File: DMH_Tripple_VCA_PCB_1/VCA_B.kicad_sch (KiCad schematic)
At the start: 19 parts, among them Q3 BC548, Q4 BC548, U1 TL074

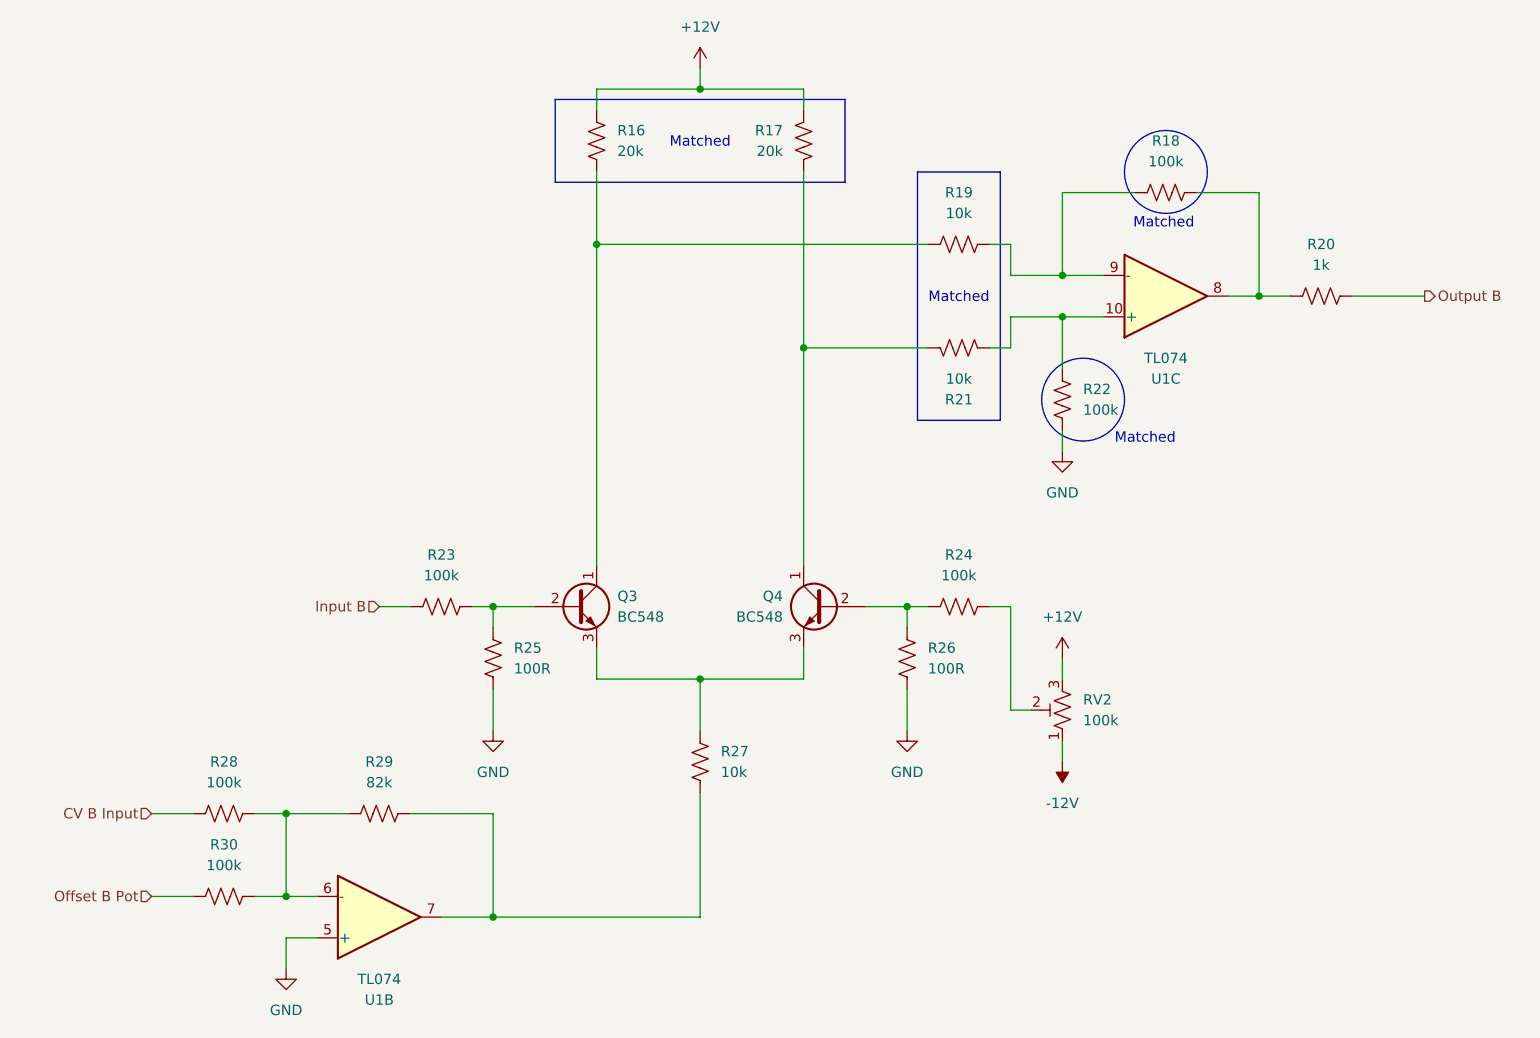
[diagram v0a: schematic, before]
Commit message: PCB 1 component positioning in progress
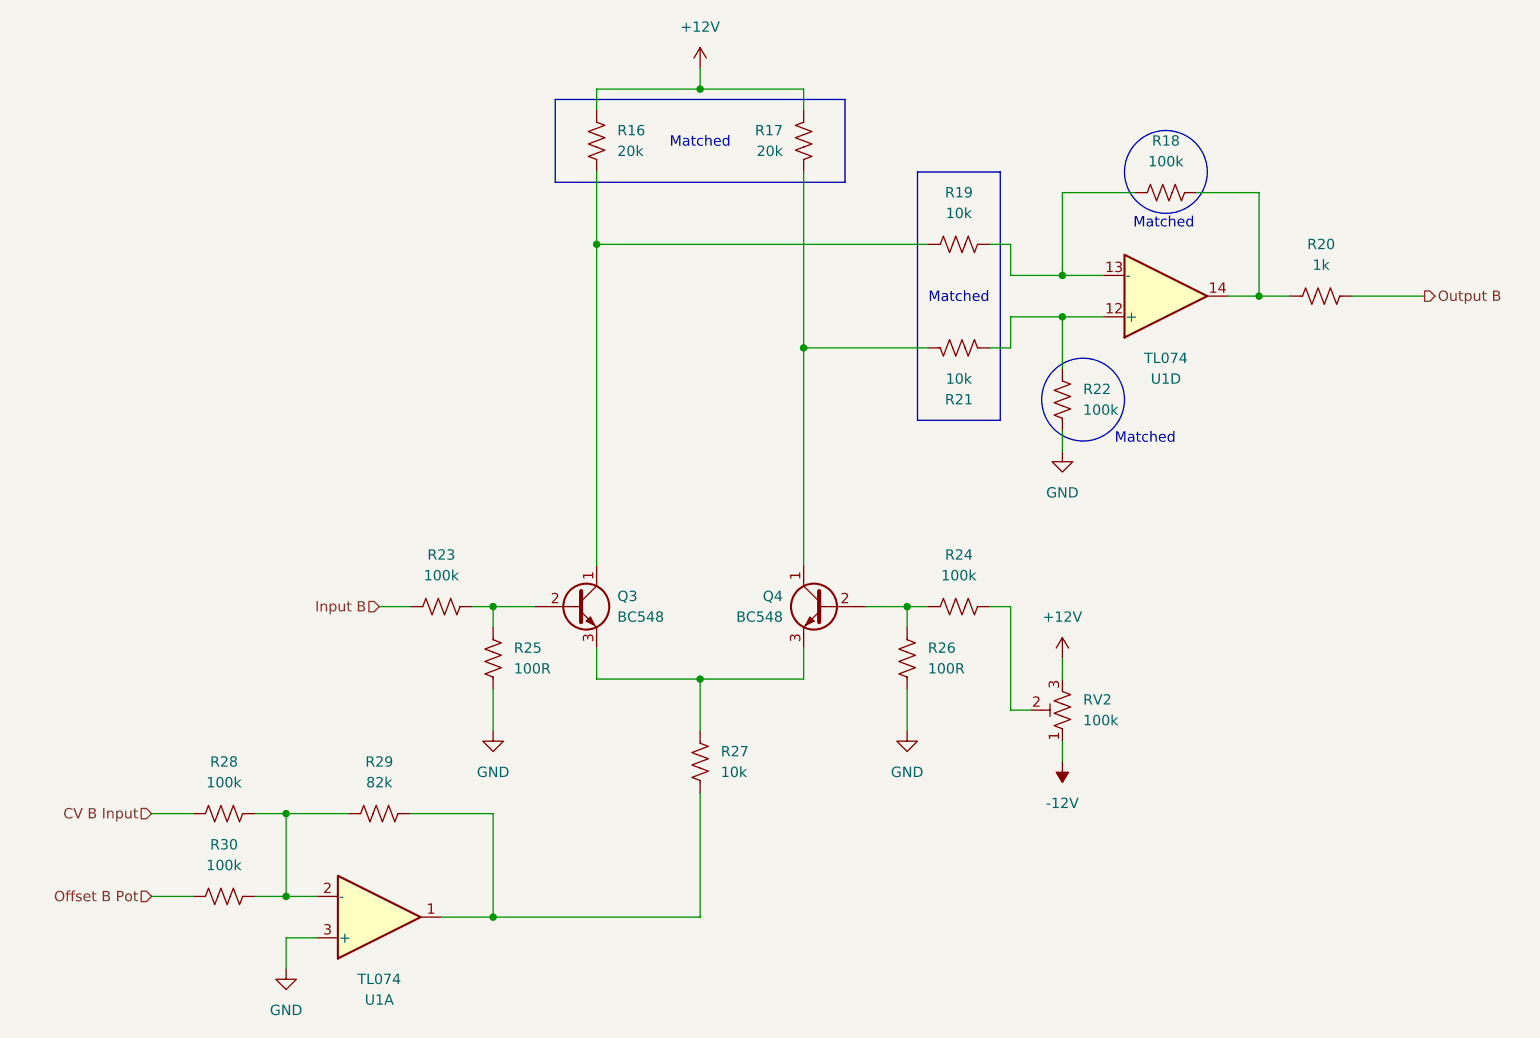
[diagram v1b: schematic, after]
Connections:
- net GND: now also U1.3 (+); no longer U1.5 (+)
- net at R18.1, R20.2: now also U1.14; no longer U1.8
- net at R18.2, R19.1: now also U1.13 (-); no longer U1.9 (-)
- net at R21.1, R22.1: now also U1.12 (+); no longer U1.10 (+)
- net at R28.2, R29.1, R30.2: now also U1.2 (-); no longer U1.6 (-)
- net at R27.1, R29.2: now also U1.1; no longer U1.7
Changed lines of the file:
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@@
 		(at 184.15 76.2 0)
 		(mirror x)
-		(unit 3)
+		(unit 4)
 		(exclude_from_sim no)
 		(in_bom yes)
@@
 				(path "/58f4306d-5387-4983-bb08-41a2313fd315/b1c4e848-8fe8-4310-abec-b04b02b54b3f"
 					(reference "U1")
-					(unit 3)
+					(unit 4)
 				)
 			)
@@
 		(at 87.63 152.4 0)
 		(mirror x)
-		(unit 2)
+		(unit 1)
 		(exclude_from_sim no)
 		(in_bom yes)
@@
 				(path "/58f4306d-5387-4983-bb08-41a2313fd315/b1c4e848-8fe8-4310-abec-b04b02b54b3f"
 					(reference "U1")
-					(unit 2)
+					(unit 1)
 				)
 			)

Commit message: Adjusted OpAmp pinouts for placement
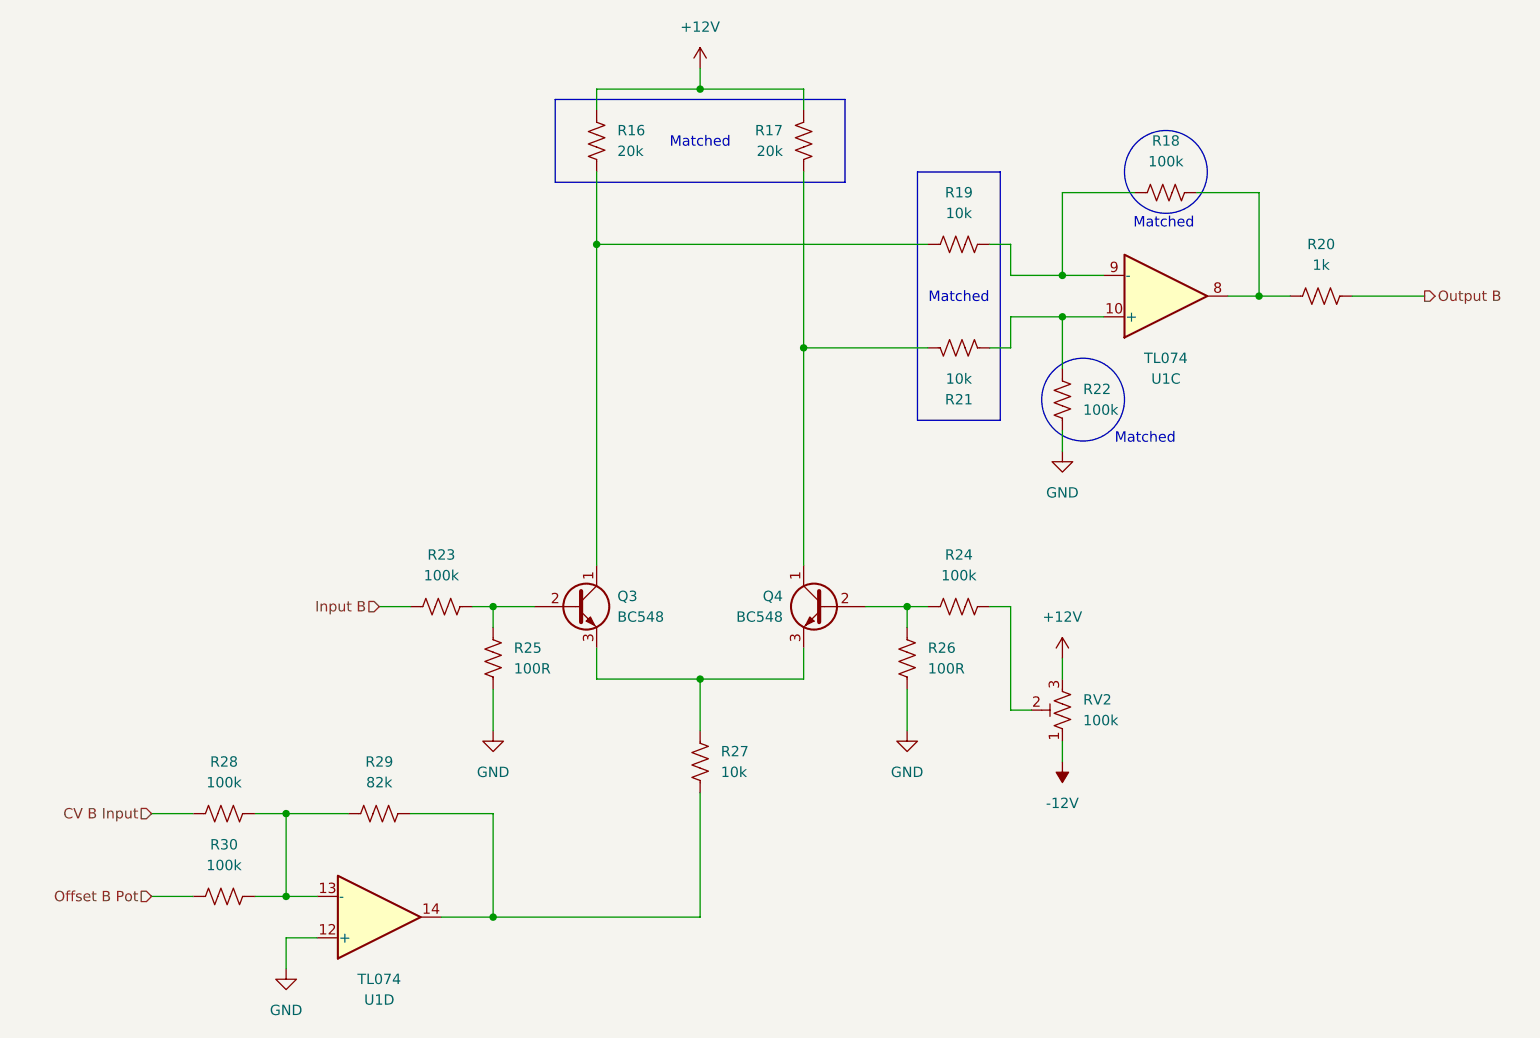
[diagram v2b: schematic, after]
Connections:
- net GND: now also U1.12 (+); no longer U1.3 (+)
- net at R18.1, R20.2: now also U1.8; no longer U1.14
- net at R18.2, R19.1: now also U1.9 (-); no longer U1.13 (-)
- net at R21.1, R22.1: now also U1.10 (+); no longer U1.12 (+)
- net at R27.1, R29.2: now also U1.14; no longer U1.1
- net at R28.2, R29.1, R30.2: now also U1.13 (-); no longer U1.2 (-)
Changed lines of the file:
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@@
 		(at 184.15 76.2 0)
 		(mirror x)
-		(unit 4)
+		(unit 3)
 		(exclude_from_sim no)
 		(in_bom yes)
@@
 				(path "/58f4306d-5387-4983-bb08-41a2313fd315/b1c4e848-8fe8-4310-abec-b04b02b54b3f"
 					(reference "U1")
-					(unit 4)
+					(unit 3)
 				)
 			)
@@
 		(at 87.63 152.4 0)
 		(mirror x)
-		(unit 1)
+		(unit 4)
 		(exclude_from_sim no)
 		(in_bom yes)
@@
 				(path "/58f4306d-5387-4983-bb08-41a2313fd315/b1c4e848-8fe8-4310-abec-b04b02b54b3f"
 					(reference "U1")
-					(unit 1)
+					(unit 4)
 				)
 			)

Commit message: Started routing over with upright resistor fps
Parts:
- R16, R17, R18, R19, R20, R21, R22, R23, R24, R25, R26, R27, R28, R29, R30: footprint Resistor_THT:R_Axial_DIN0207_L6.3mm_D2.5mm_P7.62mm_Horizontal -> Resistor_THT:R_Axial_DIN0207_L6.3mm_D2.5mm_P2.54mm_Vertical
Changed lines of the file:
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@@
 			)
 		)
-		(property "Footprint" "Resistor_THT:R_Axial_DIN0207_L6.3mm_D2.5mm_P7.62mm_Horizontal"
+		(property "Footprint" "Resistor_THT:R_Axial_DIN0207_L6.3mm_D2.5mm_P2.54mm_Vertical"
 			(at 183.896 64.516 90)
 			(effects
@@
 			)
 		)
-		(property "Footprint" "Resistor_THT:R_Axial_DIN0207_L6.3mm_D2.5mm_P7.62mm_Horizontal"
+		(property "Footprint" "Resistor_THT:R_Axial_DIN0207_L6.3mm_D2.5mm_P2.54mm_Vertical"
 			(at 151.384 120.396 90)
 			(effects
@@
 			)
 		)
-		(property "Footprint" "Resistor_THT:R_Axial_DIN0207_L6.3mm_D2.5mm_P7.62mm_Horizontal"
+		(property "Footprint" "Resistor_THT:R_Axial_DIN0207_L6.3mm_D2.5mm_P2.54mm_Vertical"
 			(at 202.946 77.216 90)
 			(effects
@@
 			)
 		)
-		(property "Footprint" "Resistor_THT:R_Axial_DIN0207_L6.3mm_D2.5mm_P7.62mm_Horizontal"
+		(property "Footprint" "Resistor_THT:R_Axial_DIN0207_L6.3mm_D2.5mm_P2.54mm_Vertical"
 			(at 100.584 120.396 90)
 			(effects
@@
 			)
 		)
-		(property "Footprint" "Resistor_THT:R_Axial_DIN0207_L6.3mm_D2.5mm_P7.62mm_Horizontal"
+		(property "Footprint" "Resistor_THT:R_Axial_DIN0207_L6.3mm_D2.5mm_P2.54mm_Vertical"
 			(at 158.496 81.534 90)
 			(effects
@@
 			)
 		)
-		(property "Footprint" "Resistor_THT:R_Axial_DIN0207_L6.3mm_D2.5mm_P7.62mm_Horizontal"
+		(property "Footprint" "Resistor_THT:R_Axial_DIN0207_L6.3mm_D2.5mm_P2.54mm_Vertical"
 			(at 94.996 115.316 90)
 			(effects
@@
 			)
 		)
-		(property "Footprint" "Resistor_THT:R_Axial_DIN0207_L6.3mm_D2.5mm_P7.62mm_Horizontal"
+		(property "Footprint" "Resistor_THT:R_Axial_DIN0207_L6.3mm_D2.5mm_P2.54mm_Vertical"
 			(at 113.284 56.896 90)
 			(effects
@@
 			)
 		)
-		(property "Footprint" "Resistor_THT:R_Axial_DIN0207_L6.3mm_D2.5mm_P7.62mm_Horizontal"
+		(property "Footprint" "Resistor_THT:R_Axial_DIN0207_L6.3mm_D2.5mm_P2.54mm_Vertical"
 			(at 158.496 115.316 90)
 			(effects
@@
 			)
 		)
-		(property "Footprint" "Resistor_THT:R_Axial_DIN0207_L6.3mm_D2.5mm_P7.62mm_Horizontal"
+		(property "Footprint" "Resistor_THT:R_Axial_DIN0207_L6.3mm_D2.5mm_P2.54mm_Vertical"
 			(at 158.496 70.866 90)
 			(effects
@@
 			)
 		)
-		(property "Footprint" "Resistor_THT:R_Axial_DIN0207_L6.3mm_D2.5mm_P7.62mm_Horizontal"
+		(property "Footprint" "Resistor_THT:R_Axial_DIN0207_L6.3mm_D2.5mm_P2.54mm_Vertical"
 			(at 87.884 138.684 90)
 			(effects
@@
 			)
 		)
-		(property "Footprint" "Resistor_THT:R_Axial_DIN0207_L6.3mm_D2.5mm_P7.62mm_Horizontal"
+		(property "Footprint" "Resistor_THT:R_Axial_DIN0207_L6.3mm_D2.5mm_P2.54mm_Vertical"
 			(at 172.466 89.154 90)
 			(effects
@@
 			)
 		)
-		(property "Footprint" "Resistor_THT:R_Axial_DIN0207_L6.3mm_D2.5mm_P7.62mm_Horizontal"
+		(property "Footprint" "Resistor_THT:R_Axial_DIN0207_L6.3mm_D2.5mm_P2.54mm_Vertical"
 			(at 68.834 138.684 90)
 			(effects
@@
 			)
 		)
-		(property "Footprint" "Resistor_THT:R_Axial_DIN0207_L6.3mm_D2.5mm_P7.62mm_Horizontal"
+		(property "Footprint" "Resistor_THT:R_Axial_DIN0207_L6.3mm_D2.5mm_P2.54mm_Vertical"
 			(at 68.834 148.844 90)
 			(effects
@@
 			)
 		)
-		(property "Footprint" "Resistor_THT:R_Axial_DIN0207_L6.3mm_D2.5mm_P7.62mm_Horizontal"
+		(property "Footprint" "Resistor_THT:R_Axial_DIN0207_L6.3mm_D2.5mm_P2.54mm_Vertical"
 			(at 140.716 56.896 90)
 			(effects
@@
 			)
 		)
-		(property "Footprint" "Resistor_THT:R_Axial_DIN0207_L6.3mm_D2.5mm_P7.62mm_Horizontal"
+		(property "Footprint" "Resistor_THT:R_Axial_DIN0207_L6.3mm_D2.5mm_P2.54mm_Vertical"
 			(at 125.984 133.096 90)
 			(effects

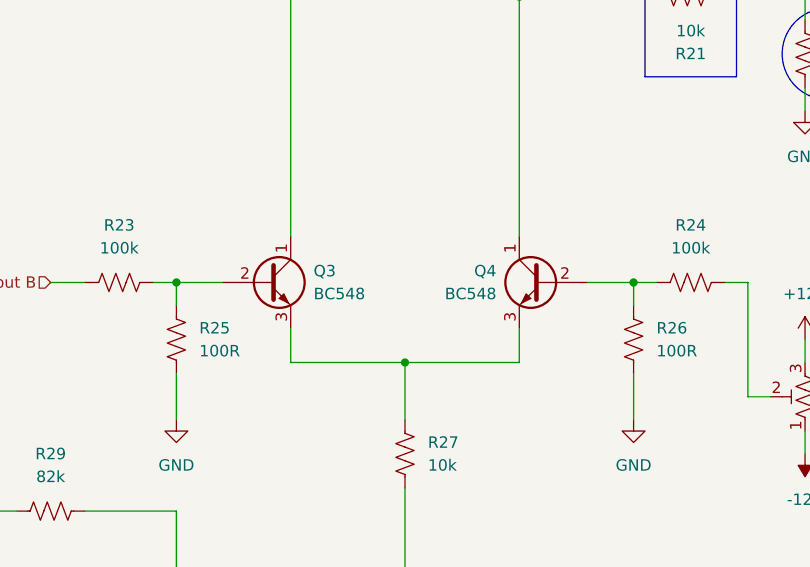
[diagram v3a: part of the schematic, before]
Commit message: Converted PCB 1 project to KiCad 9
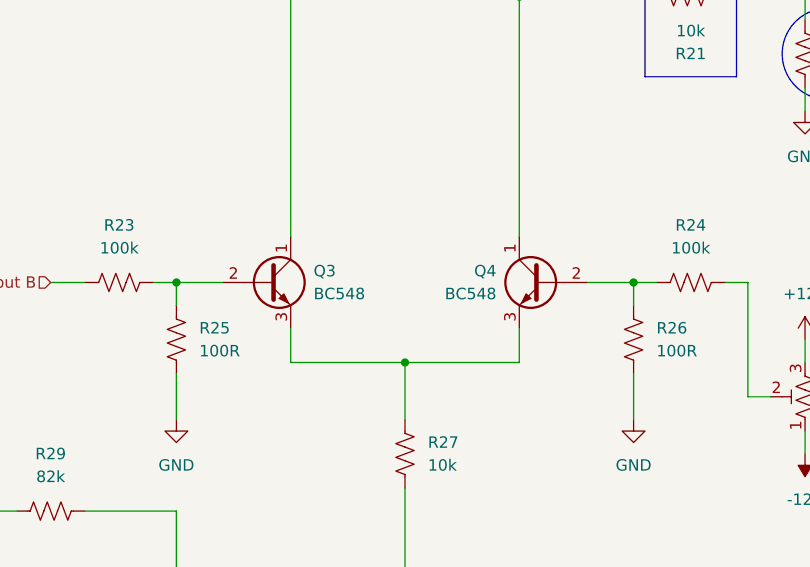
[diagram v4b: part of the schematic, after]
